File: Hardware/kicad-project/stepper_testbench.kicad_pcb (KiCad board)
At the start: 2 copper layers, 67.7 x 76.7 mm, 77 parts, among them CN10 Conn_02x17_Odd_Even, CN7 Conn_02x10_Odd_Even, CN8 Conn_02x08_Odd_Even, CN9 Conn_02x15_Odd_Even, J1 Brake connector, J2 Conn_01x08, J3 PWM module connector, J4 Conn_01x02, J5 UART Connector, J6 Stepper supply, Q1 Q_NMOS_DGS, U1 LM358P, U2 LEM-CAS-6NP, U3 LM358P, U4 LM358P, U5 LM7812_TO220, U6 L7805

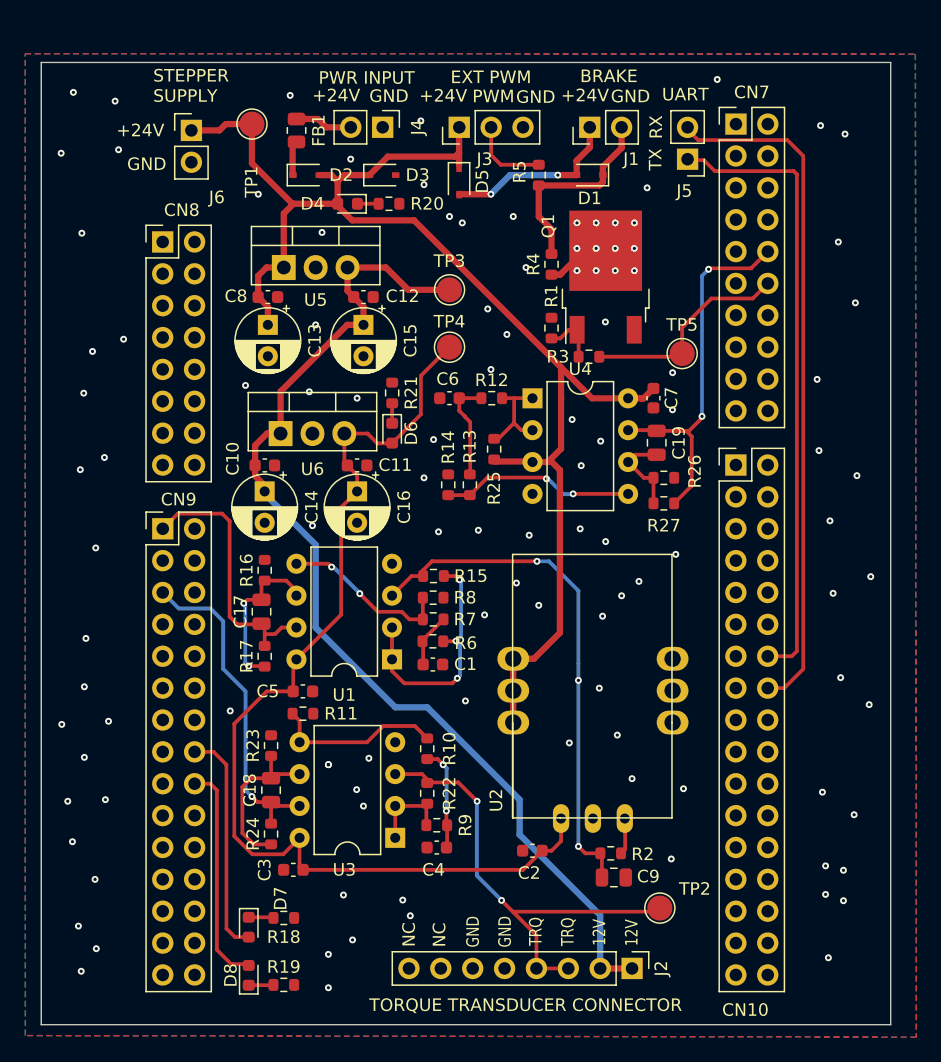
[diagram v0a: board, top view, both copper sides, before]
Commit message: hw: add round corners and credits
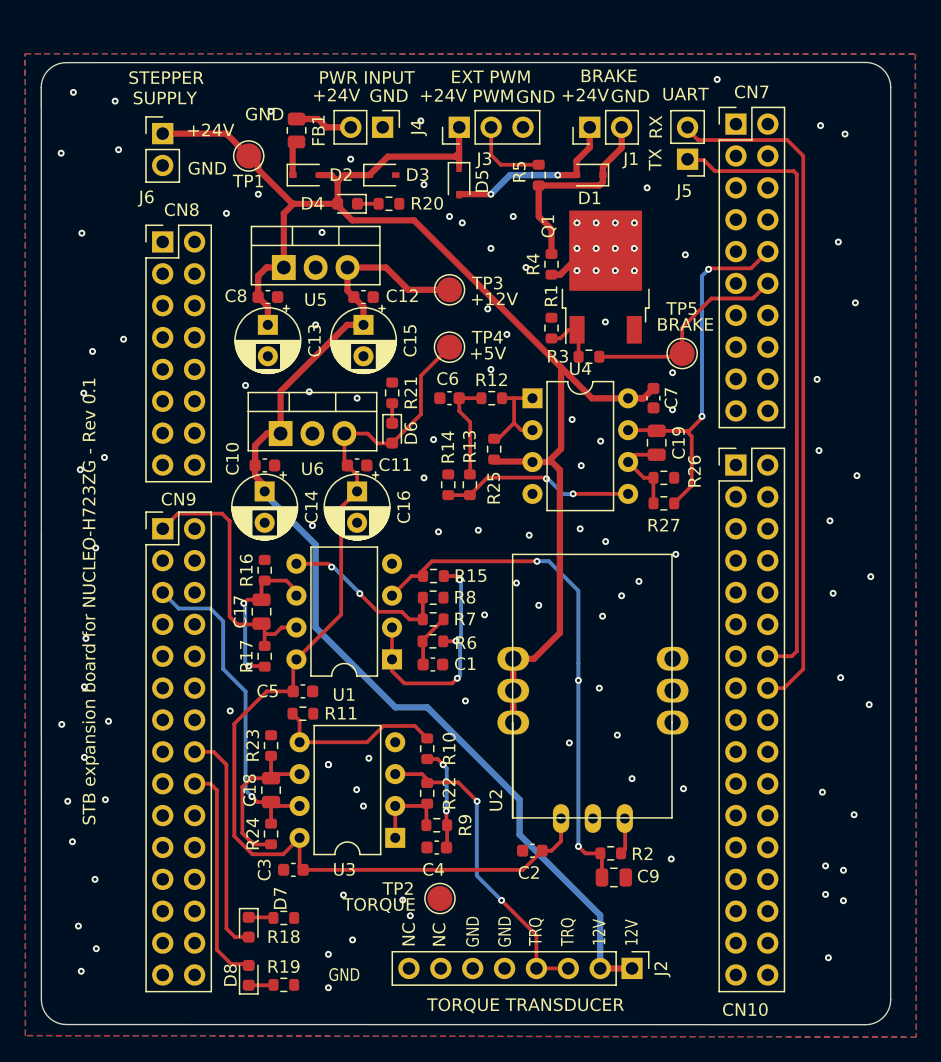
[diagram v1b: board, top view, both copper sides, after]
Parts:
- moved TP2 17.5 mm to (142.2, 130.3)
- moved TP1 2.55 mm to (127.0, 71.1)
- moved J6 2.30 mm to (120.1, 69.3)
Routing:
- net /Connectors/TORQUE: track 37.4 -> 25.5 mm
- net GND: vias 96 -> 99
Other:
- outline, holes or cut-outs redrawn
- board text added: "+12V"
- board text added: "+5V"
- board text added: "@ProM Facility, Rovereto Designed by Canova Tommaso, Santarossa Lisa"
- board text added: "STB expansion board for NUCLEO-H723ZG - Rev 0.1"
- board text added: "STEPPER"
- board text added: "SUPPLY"
- board text added: "TORQUE"
- board text added: "TORQUE TRANSDUCER"
- board text removed: "STEPPER SUPPLY"
- board text removed: "TORQUE TRANSDUCER CONNECTOR"

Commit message: hw: update layout with right screw terminal
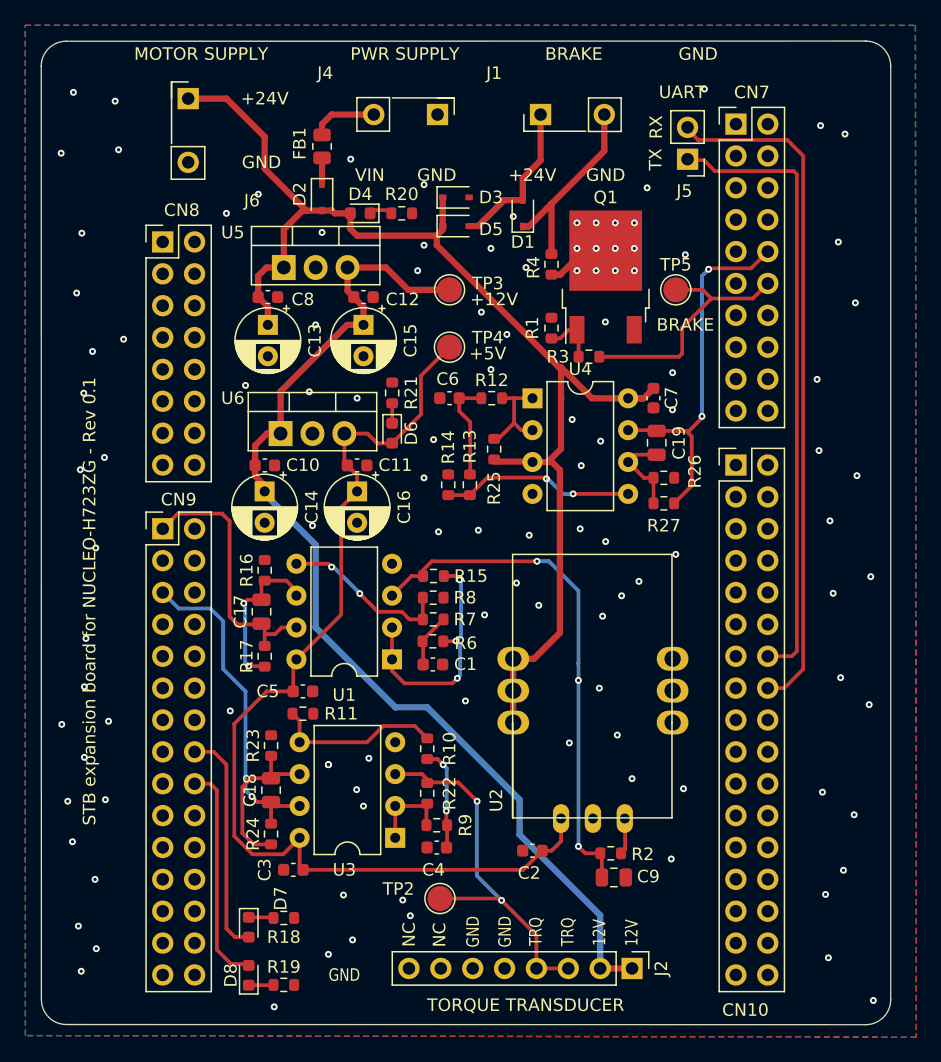
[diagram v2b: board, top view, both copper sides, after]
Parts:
- removed J3: PWM module connector, Connector_PinHeader_2.54mm:PinHeader_1x03_P2.54mm_Vertical
- removed R5: 0, Resistor_SMD:R_0603_1608Metric
- removed TP1: 24V, TestPoint:TestPoint_Pad_D2.0mm
- moved D1 6.14 mm to (148.8, 75.7), turned to 90 degrees
- moved D3 6.11 mm to (143.5, 74.4)
- moved TP5 5.11 mm to (161.0, 81.8)
- moved J4 4.49 mm to (142.0, 67.8)
- moved J1 4.05 mm to (150.3, 67.8)
- moved D5 3.57 mm to (143.5, 76.7), turned to 0 degrees
- moved J6 3.45 mm to (122.2, 66.5)
- moved FB1 2.40 mm to (132.8, 70.4)
- moved D2 2.18 mm to (132.8, 74.4), turned to -90 degrees
- moved R20 1.27 mm to (139.2, 75.7)
- moved D4 1.27 mm to (135.9, 75.7)
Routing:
- net +24V: track 113.6 -> 101.3 mm
- net Net-(J3-Pad2): track 6.33 -> 0.00 mm
- net /Connectors/TORQUE: track 25.5 -> 30.5 mm
- net /Connectors/PWM_BRAKE: track 17.1 -> 20.2 mm
- net Net-(D1-Pad2): track 14.3 -> 12.5 mm, vias 2 -> 0
- net Net-(FB1-Pad1): track 4.60 -> 5.31 mm
- net Net-(D2-Pad1): track 2.78 -> 2.10 mm
- net GND: vias 99 -> 97
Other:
- board size 67.7 x 76.7 mm -> 67.7 x 78.4 mm
- board text added: "MOTOR SUPPLY"
- board text added: "PWR SUPPLY"
- board text added: "VIN"
- board text removed: "EXT PWM"
- board text removed: "PWM"
- board text removed: "PWR INPUT"
- board text removed: "STEPPER"
- board text removed: "SUPPLY"
- board text removed: "TORQUE"

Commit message: hw: update layout
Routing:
- net +12V: track 85.6 -> 84.2 mm
- net /Connectors/PWM_BRAKE: track 20.2 -> 19.0 mm
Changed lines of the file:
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@@
   (segment (start 155.01 135.875) (end 157.55 135.875) (width 0.5) (layer "F.Cu") (net 2))
   (segment (start 136.144 83.142) (end 135.369 82.367) (width 0.5) (layer "F.Cu") (net 2))
-  (segment (start 132.334 102.108) (end 132.334 108.712) (width 0.5) (layer "B.Cu") (net 2))
+  (segment (start 128.27 98.044) (end 132.334 102.108) (width 0.5) (layer "B.Cu") (net 2))
+  (segment (start 155.01 130.372) (end 155.01 135.875) (width 0.5) (layer "B.Cu") (net 2))
   (segment (start 128.27 97.854888) (end 128.27 98.044) (width 0.5) (layer "B.Cu") (net 2))
-  (segment (start 141.224 115.062) (end 148.59 122.428) (width 0.5) (layer "B.Cu") (net 2))
-  (segment (start 148.59 122.428) (end 148.59 125.222) (width 0.5) (layer "B.Cu") (net 2))
-  (segment (start 138.684 115.062) (end 141.224 115.062) (width 0.5) (layer "B.Cu") (net 2))
-  (segment (start 128.27 98.044) (end 132.334 102.108) (width 0.5) (layer "B.Cu") (net 2))
-  (segment (start 132.334 108.712) (end 138.684 115.062) (width 0.5) (layer "B.Cu") (net 2))
-  (segment (start 155.01 131.642) (end 155.01 135.875) (width 0.5) (layer "B.Cu") (net 2))
-  (segment (start 148.59 125.222) (end 155.01 131.642) (width 0.5) (layer "B.Cu") (net 2))
+  (segment (start 132.334 107.696) (end 155.01 130.372) (width 0.5) (layer "B.Cu") (net 2))
+  (segment (start 132.334 102.108) (end 132.334 107.696) (width 0.5) (layer "B.Cu") (net 2))
   (segment (start 143.625 112.75) (end 143.225 113.15) (width 0.3) (layer "F.Cu") (net 3))
   (segment (start 143.525 109.775) (end 143.5 109.8) (width 0.3) (layer "F.Cu") (net 3))
@@
   (segment (start 169.677 113.533) (end 168.365 113.533) (width 0.3) (layer "F.Cu") (net 11))
   (segment (start 171.196 71.12) (end 171.196 112.014) (width 0.3) (layer "F.Cu") (net 11))
-  (segment (start 161.29 87.122) (end 154.94 87.122) (width 0.3) (layer "F.Cu") (net 12))
+  (segment (start 159.258 87.122) (end 154.94 87.122) (width 0.3) (layer "F.Cu") (net 12))
   (segment (start 168.372 81.28) (end 167.172489 82.479511) (width 0.3) (layer "F.Cu") (net 12))
   (segment (start 167.172489 82.479511) (end 163.870489 82.479511) (width 0.3) (layer "F.Cu") (net 12))
-  (segment (start 161.544 84.806) (end 161.544 86.868) (width 0.3) (layer "F.Cu") (net 12))
   (segment (start 163.178978 81.788) (end 161.036 81.788) (width 0.3) (layer "F.Cu") (net 12))
-  (segment (start 161.544 86.868) (end 161.29 87.122) (width 0.3) (layer "F.Cu") (net 12))
+  (segment (start 163.870489 82.479511) (end 161.544 84.806) (width 0.3) (layer "F.Cu") (net 12))
+  (segment (start 161.544 84.806) (end 161.544 84.836) (width 0.3) (layer "F.Cu") (net 12))
   (segment (start 163.870489 82.479511) (end 163.178978 81.788) (width 0.3) (layer "F.Cu") (net 12))
-  (segment (start 163.870489 82.479511) (end 161.544 84.806) (width 0.3) (layer "F.Cu") (net 12))
+  (segment (start 161.544 84.836) (end 159.258 87.122) (width 0.3) (layer "F.Cu") (net 12))
   (segment (start 148.149 90.424) (end 149.606 90.424) (width 0.3) (layer "F.Cu") (net 13))
   (segment (start 148.724 92.974) (end 148.149 92.399) (width 0.3) (layer "F.Cu") (net 13))
@@
   (segment (start 141.161 122.808) (end 141.224 122.745) (width 0.3) (layer "F.Cu") (net 119))
   (segment (start 141.224 122.745) (end 141.044 122.925) (width 0.3) (layer "F.Cu") (net 119))
+  (segment (start 135.418 116.55) (end 140.235 116.55) (width 0.3) (layer "F.Cu") (net 120))
+  (segment (start 131.054 117.846) (end 131.054 116.131) (width 0.3) (layer "F.Cu") (net 120))
+  (segment (start 131.054 117.846) (end 134.122 117.846) (width 0.3) (layer "F.Cu") (net 120))
+  (segment (start 134.122 117.846) (end 135.418 116.55) (width 0.3) (layer "F.Cu") (net 120))
   (segment (start 140.235 116.55) (end 141.224 117.539) (width 0.3) (layer "F.Cu") (net 120))
-  (segment (start 131.054 117.846) (end 131.054 116.131) (width 0.3) (layer "F.Cu") (net 120))
-  (segment (start 131.054 117.846) (end 136.429 117.846) (width 0.3) (layer "F.Cu") (net 120))
-  (segment (start 136.429 117.846) (end 137.725 116.55) (width 0.3) (layer "F.Cu") (net 120))
-  (segment (start 137.725 116.55) (end 140.235 116.55) (width 0.3) (layer "F.Cu") (net 120))
   (segment (start 131.054 116.131) (end 130.493 115.57) (width 0.3) (layer "F.Cu") (net 120))
   (segment (start 151.13 74.93) (end 151.13 78.931) (width 0.5) (layer "F.Cu") (net 123))

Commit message: hw: update layout
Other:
- board text added: "STEPPER SUPPLY"
- board text removed: "MOTOR SUPPLY"
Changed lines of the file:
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@@
     (effects (font (size 1 1) (thickness 0.15)) (justify mirror))
   )
-  (gr_text "MOTOR SUPPLY\n" (at 117.856 62.992) (layer "F.SilkS")
+  (gr_text "STEPPER SUPPLY\n" (at 117.856 62.992) (layer "F.SilkS")
     (effects (font (size 1 1) (thickness 0.25)) (justify left))
   )

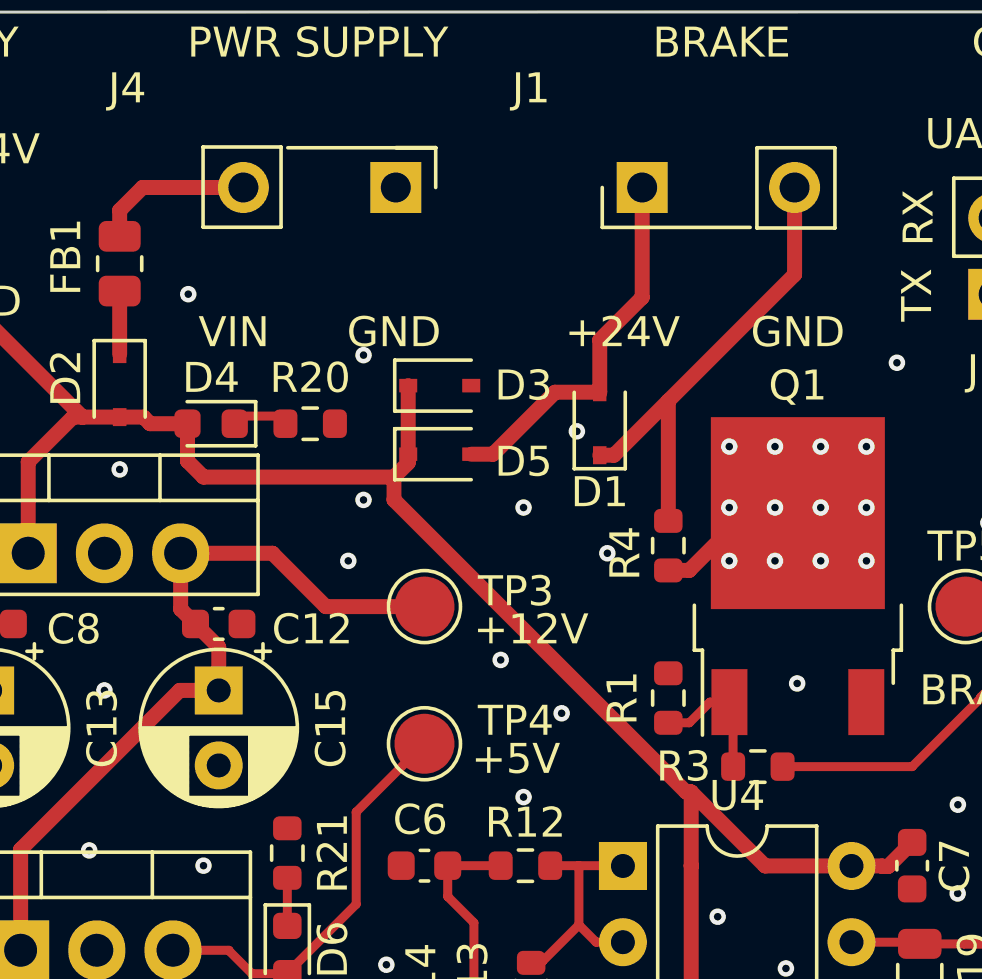
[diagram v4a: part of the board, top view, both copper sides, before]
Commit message: change 24V zener footprint to SMA
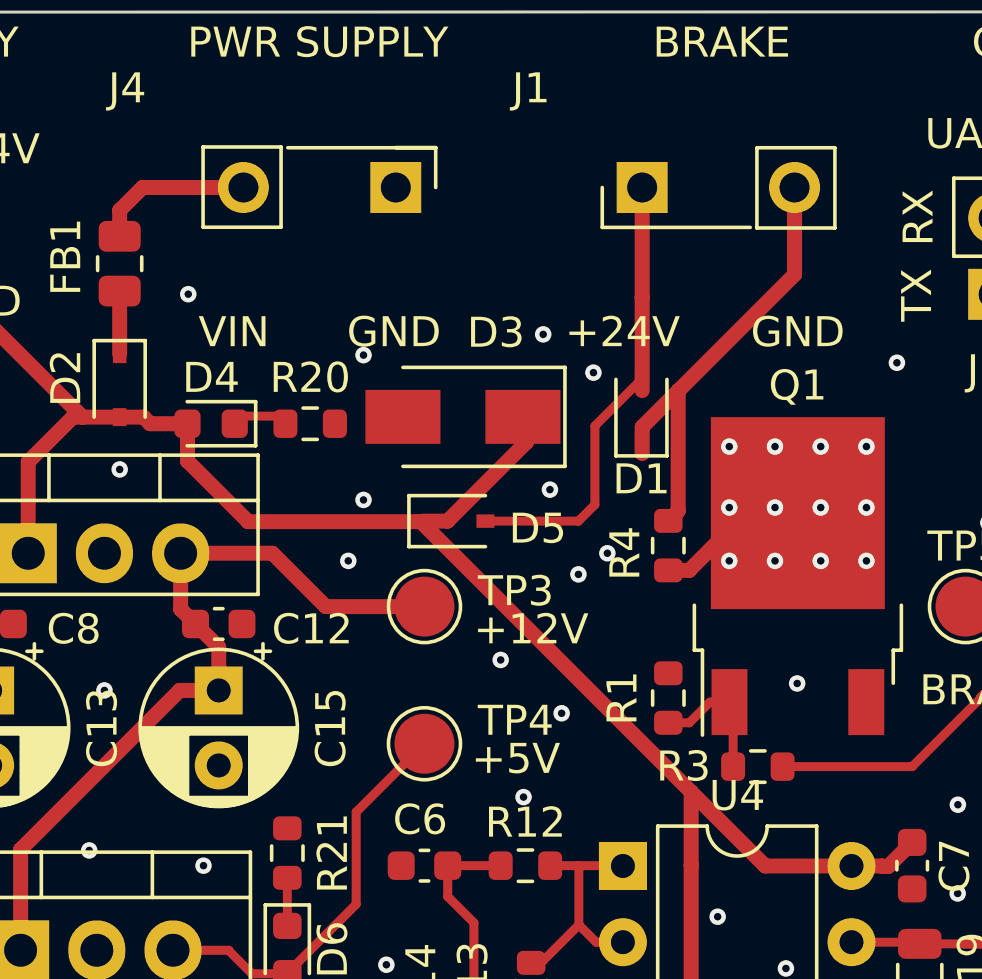
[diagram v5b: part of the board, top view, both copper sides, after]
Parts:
- D3: footprint Diode_SMD:D_SOD-323 -> Diode_SMD:D_SMA
- moved D5 2.28 mm to (144.0, 78.9)
- moved D1 1.45 mm to (150.2, 75.3)
- moved D3 1.30 mm to (144.3, 75.5), turned to 180 degrees
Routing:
- net Net-(D1-Pad2): track 12.5 -> 15.5 mm
- net +24V: track 101.3 -> 103.0 mm
- net GND: vias 97 -> 99
